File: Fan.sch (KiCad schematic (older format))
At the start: 17 parts, among them Q2 DMN65D8L-7, Q3 AOD476, Q4 AOD476, U4 OPA4170, U5 MCP4801

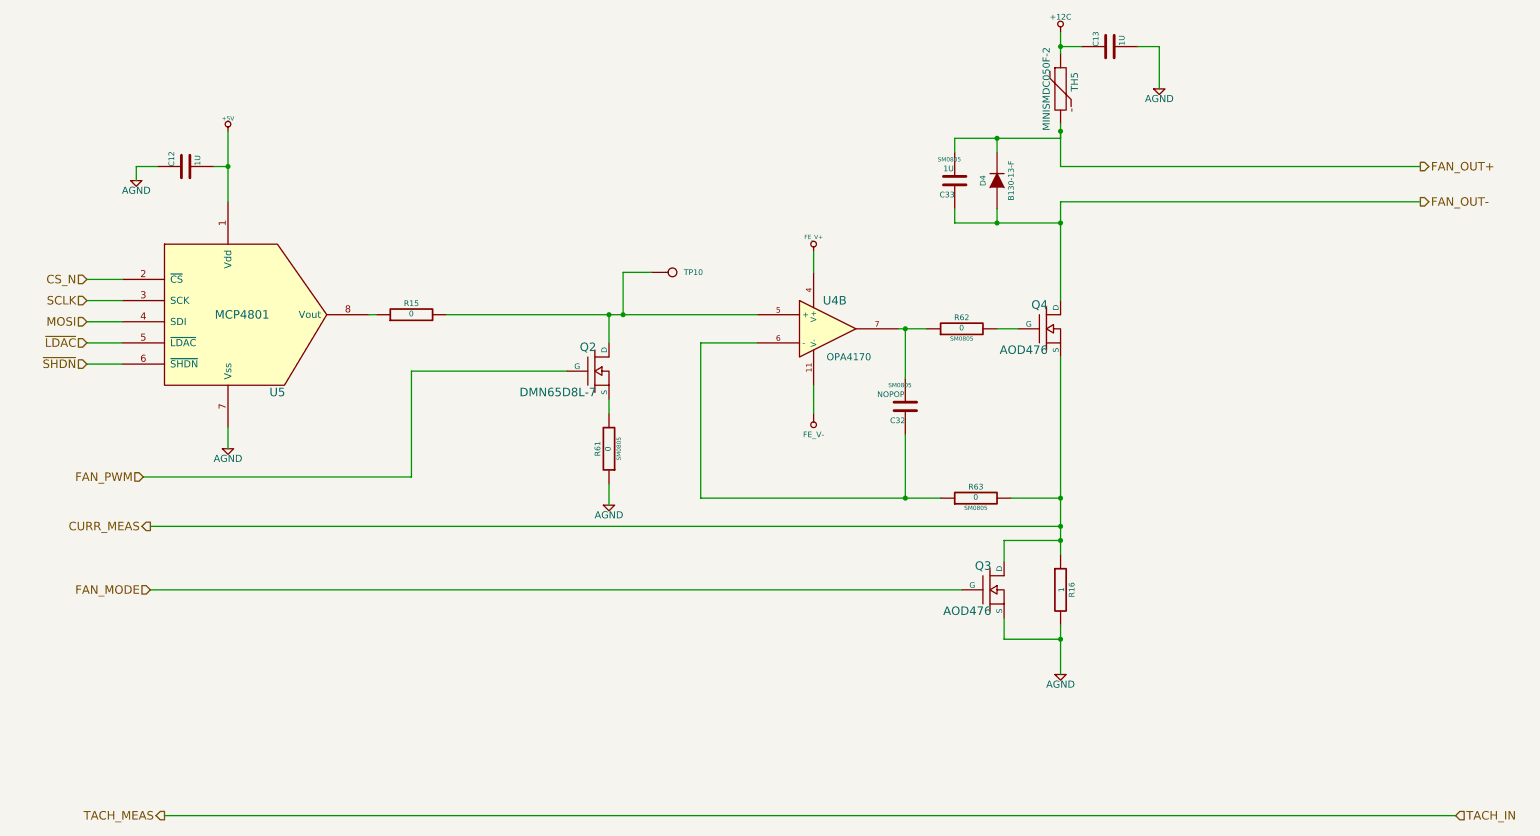
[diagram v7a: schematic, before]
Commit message: Added the schematic and BOM changes back in after hard reset
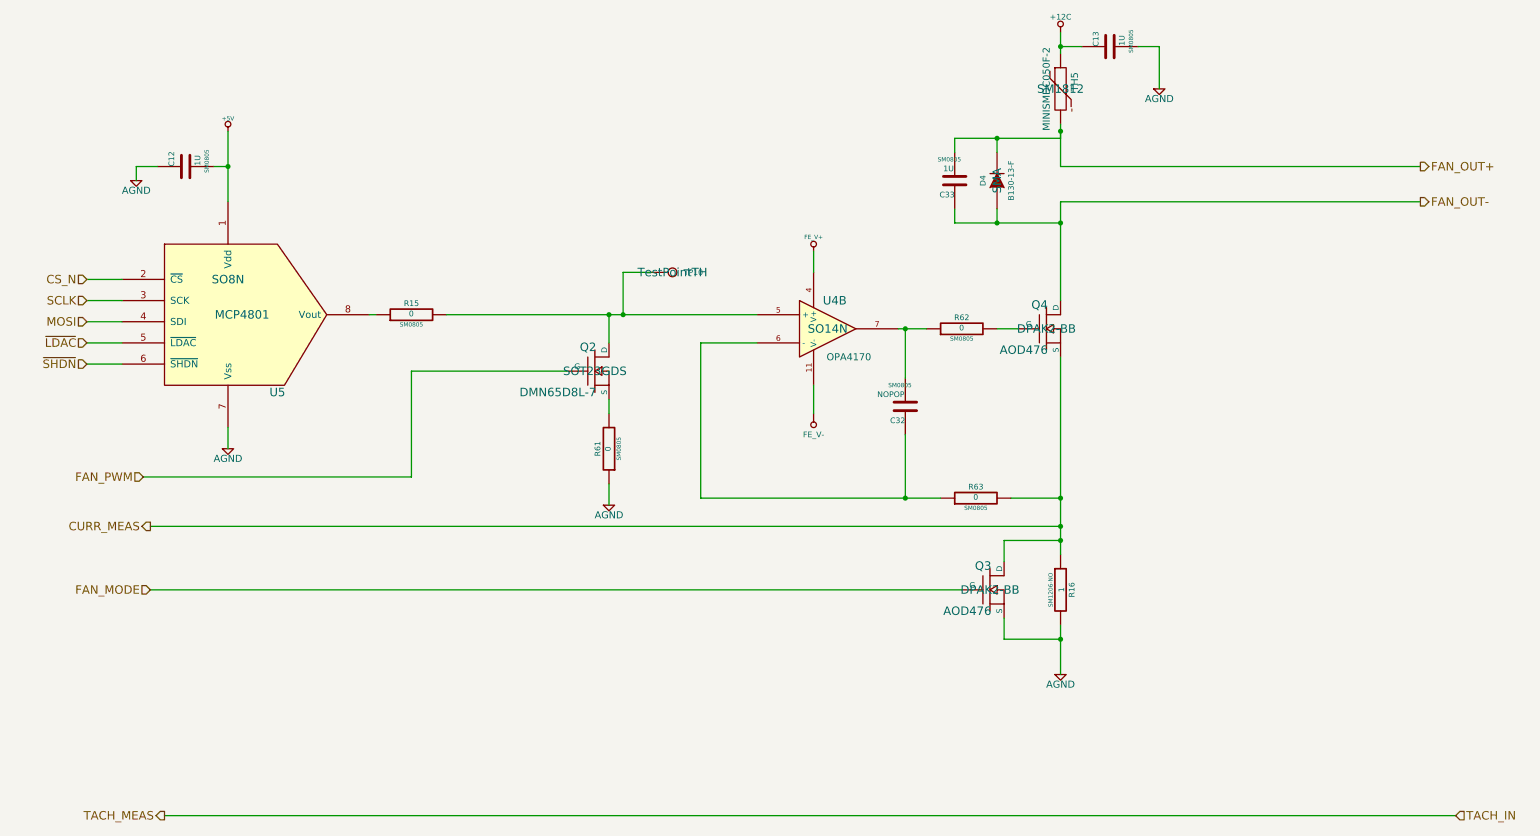
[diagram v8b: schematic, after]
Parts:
- C12, C13, R15: footprint ~ -> SM0805
- D4: footprint ~ -> SMA
- Q2: footprint ~ -> SOT23GDS
- Q3, Q4: footprint ~ -> DPAK2-BB
- R16: footprint ~ -> SM1206-NO
- TH5: footprint ~ -> SM1812
- TP10: footprint (none) -> TestPointTH
- U4: footprint (none) -> SO14N
- U5: footprint (none) -> SO8N
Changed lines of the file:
@@
-EESchema Schematic File Version 2  date 4/16/2014 11:04:06 PM
+EESchema Schematic File Version 2  date 4/18/2014 9:49:53 PM
 LIBS:power
 LIBS:device
@@
 Sheet 6 9
 Title ""
-Date "17 apr 2014"
+Date "19 apr 2014"
 Rev ""
 Comp ""
@@
 F 0 "U4" H 6300 3300 60  0000 C CNN
 F 1 "OPA4170" H 6400 2900 50  0000 C CNN
-F 2 "" H 6250 3100 60  0000 C CNN
+F 2 "SO14N" H 6250 3100 60  0000 C CNN
 F 3 "" H 6250 3100 60  0000 C CNN
 	2    6250 3100
@@
 F 0 "R16" V 7980 4950 40  0000 C CNN
 F 1 "1" V 7907 4951 40  0000 C CNN
-F 2 "~" V 7830 4950 30  0000 C CNN
+F 2 "SM1206-NO" V 7830 4950 30  0000 C CNN
 F 3 "~" H 7900 4950 30  0000 C CNN
 	1    7900 4950
@@
 F 0 "R15" V 3380 3000 40  0000 C CNN
 F 1 "0" V 3307 3001 40  0000 C CNN
-F 2 "~" V 3230 3000 30  0000 C CNN
+F 2 "SM0805" V 3230 3000 30  0000 C CNN
 F 3 "~" H 3300 3000 30  0000 C CNN
 	1    3300 3000
@@
 F 0 "TH5" V 8000 1450 50  0000 C CNN
 F 1 "MINISMDC050F-2" V 7800 1400 50  0000 C CNN
-F 2 "~" H 7900 1400 60  0000 C CNN
+F 2 "SM1812" H 7900 1400 60  0000 C CNN
 F 3 "~" H 7900 1400 60  0000 C CNN
 F 4 "TE Connectivity" H 7900 1400 60  0001 C CNN "MFG Name"
@@
 F 0 "D4" H 7450 2150 40  0000 C CNN
 F 1 "B130-13-F" H 7450 1950 40  0000 C CNN
-F 2 "~" H 7450 2050 60  0000 C CNN
+F 2 "SMA" H 7450 2050 60  0000 C CNN
 F 3 "~" H 7450 2050 60  0000 C CNN
 F 4 "Diodes Inc" H 7450 2050 60  0001 C CNN "MFG Name"
@@
 F 0 "Q2" H 4610 3570 60  0000 R CNN
 F 1 "DMN65D8L-7" H 4610 3250 60  0000 R CNN
-F 2 "~" H 4600 3400 60  0000 C CNN
+F 2 "SOT23GDS" H 4600 3400 60  0000 C CNN
 F 3 "~" H 4600 3400 60  0000 C CNN
 F 4 "Diodes Inc" H 4600 3400 60  0001 C CNN "MFG Name"
@@
 F 0 "U5" H 2350 1950 60  0000 C CNN
 F 1 "MCP4801" H 2100 2500 60  0000 C CNN
-F 2 "" H 2000 2750 60  0000 C CNN
+F 2 "SO8N" H 2000 2750 60  0000 C CNN
 F 3 "" H 2000 2750 60  0000 C CNN
 	1    2000 2750
@@
 F 0 "C12" H 1700 2050 40  0000 L CNN
 F 1 "1U" H 1706 1865 40  0000 L CNN
-F 2 "~" H 1738 1800 30  0000 C CNN
+F 2 "SM0805" H 1738 1800 30  0000 C CNN
 F 3 "~" H 1700 1950 60  0000 C CNN
 	1    1700 1950
@@
 F 0 "C13" H 8250 1200 40  0000 L CNN
 F 1 "1U" H 8256 1015 40  0000 L CNN
-F 2 "~" H 8288 950 30  0000 C CNN
+F 2 "SM0805" H 8288 950 30  0000 C CNN
 F 3 "~" H 8250 1100 60  0000 C CNN
 	1    8250 1100
@@
 F 0 "Q4" H 7810 3270 60  0000 R CNN
 F 1 "AOD476" H 7810 2950 60  0000 R CNN
-F 2 "~" H 7800 3100 60  0000 C CNN
+F 2 "DPAK2-BB" H 7800 3100 60  0000 C CNN
 F 3 "~" H 7800 3100 60  0000 C CNN
 F 4 "Alpha and Omega" H 7800 3100 60  0001 C CNN "MFG Name"
@@
 F 0 "Q3" H 7410 5120 60  0000 R CNN
 F 1 "AOD476" H 7410 4800 60  0000 R CNN
-F 2 "~" H 7400 4950 60  0000 C CNN
+F 2 "DPAK2-BB" H 7400 4950 60  0000 C CNN
 F 3 "~" H 7400 4950 60  0000 C CNN
 F 4 "Alpha and Omega" H 7400 4950 60  0001 C CNN "MFG Name"
@@
 F 0 "TP10" H 5230 2700 40  0000 L CNN
 F 1 "DAC_OUT" H 5150 2755 30  0001 C CNN
-F 2 "" H 5150 2700 60  0000 C CNN
+F 2 "TestPointTH" H 5150 2700 60  0000 C CNN
 F 3 "" H 5150 2700 60  0000 C CNN
 	1    5150 2700
